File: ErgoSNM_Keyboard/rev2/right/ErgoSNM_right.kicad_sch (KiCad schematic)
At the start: 21 parts, among them J1 USB_C_Receptacle_USB2.0, J2 USB_C_Receptacle_USB2.0, J3 PJ-393_TRRS_8P, J4 Conn_01x08, U1 RT9013-33GB, U2 SRV05-4

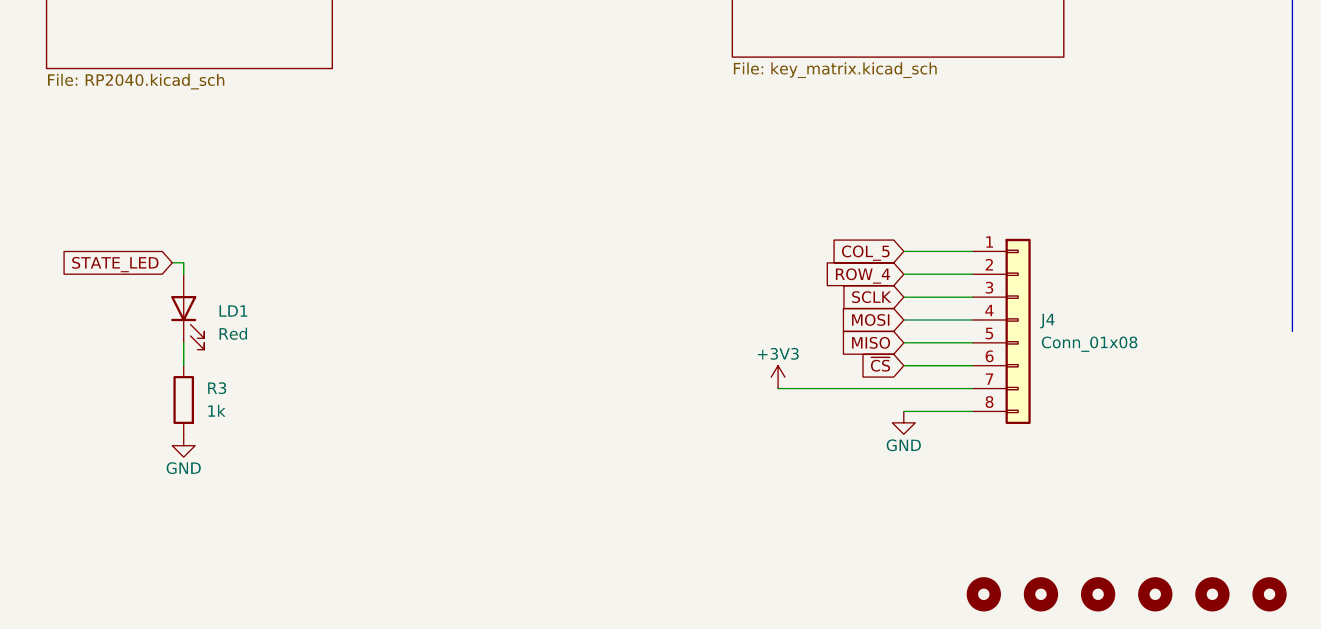
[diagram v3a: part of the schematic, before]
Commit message: Update FPC connection and add additional LED LD2
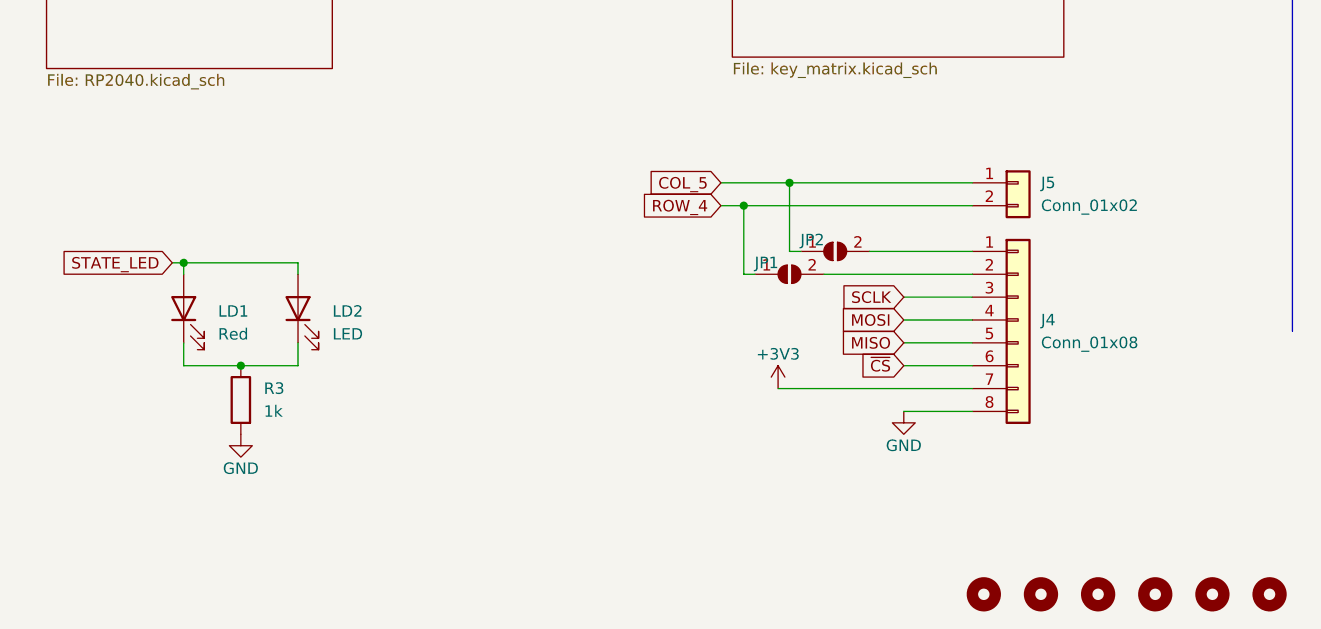
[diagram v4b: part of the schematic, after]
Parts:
- added J5: Conn_01x02, Connector_PinHeader_2.54mm:PinHeader_1x02_P2.54mm_Vertical, symbol Connector_Generic:Conn_01x02
- added JP1, JP2: SolderJumper_2_Open, Jumper:SolderJumper-2_P1.3mm_Open_TrianglePad1.0x1.5mm, symbol Jumper:SolderJumper_2_Open
- added LD2: LED, LED_SMD:LED_0805_2012Metric_Pad1.15x1.40mm_HandSolder, symbol Device:LED
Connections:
- net COL_5: now also J5.1 (Pin_1), JP2.1 (A); no longer J4.1 (Pin_1)
- net ROW_4: now also J5.2 (Pin_2), JP1.1 (A); no longer J4.2 (Pin_2)
- net STATE_LED: now also LD2.2 (A)
- net at LD1.1 (K), R3.1: now also LD2.1 (K)
- new net: J4.2 (Pin_2), JP1.2 (B)
- new net: J4.1 (Pin_1), JP2.2 (B)
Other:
- moved on the sheet: R3

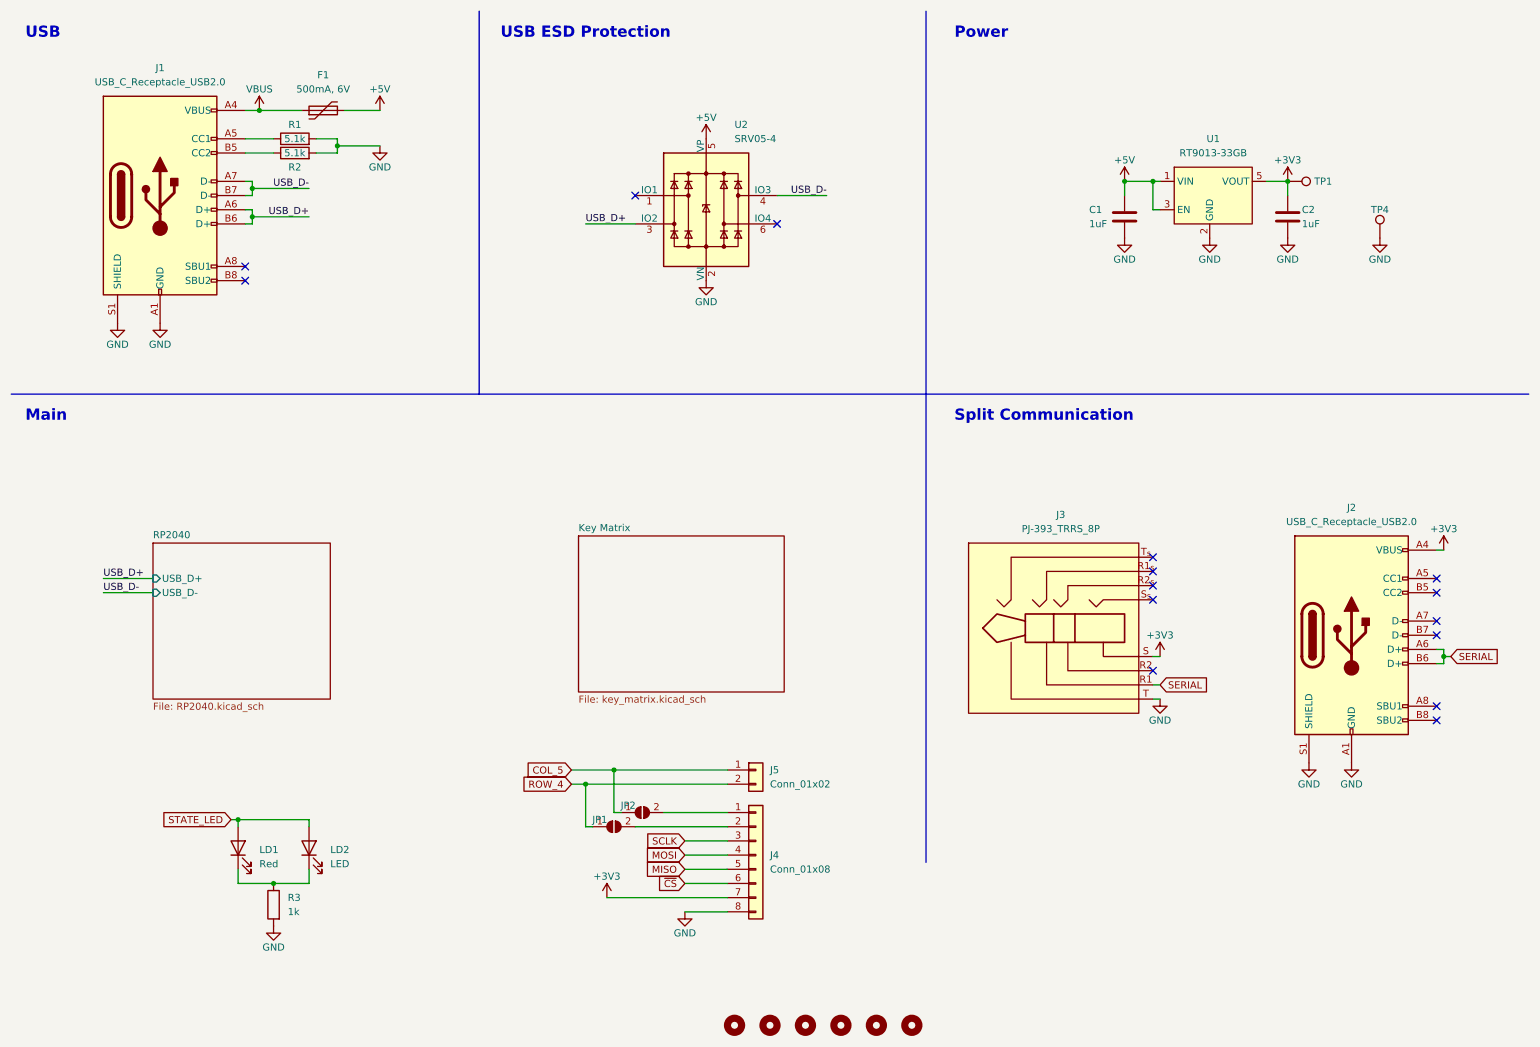
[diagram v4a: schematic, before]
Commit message: Change license to CERN-OHL-P v2
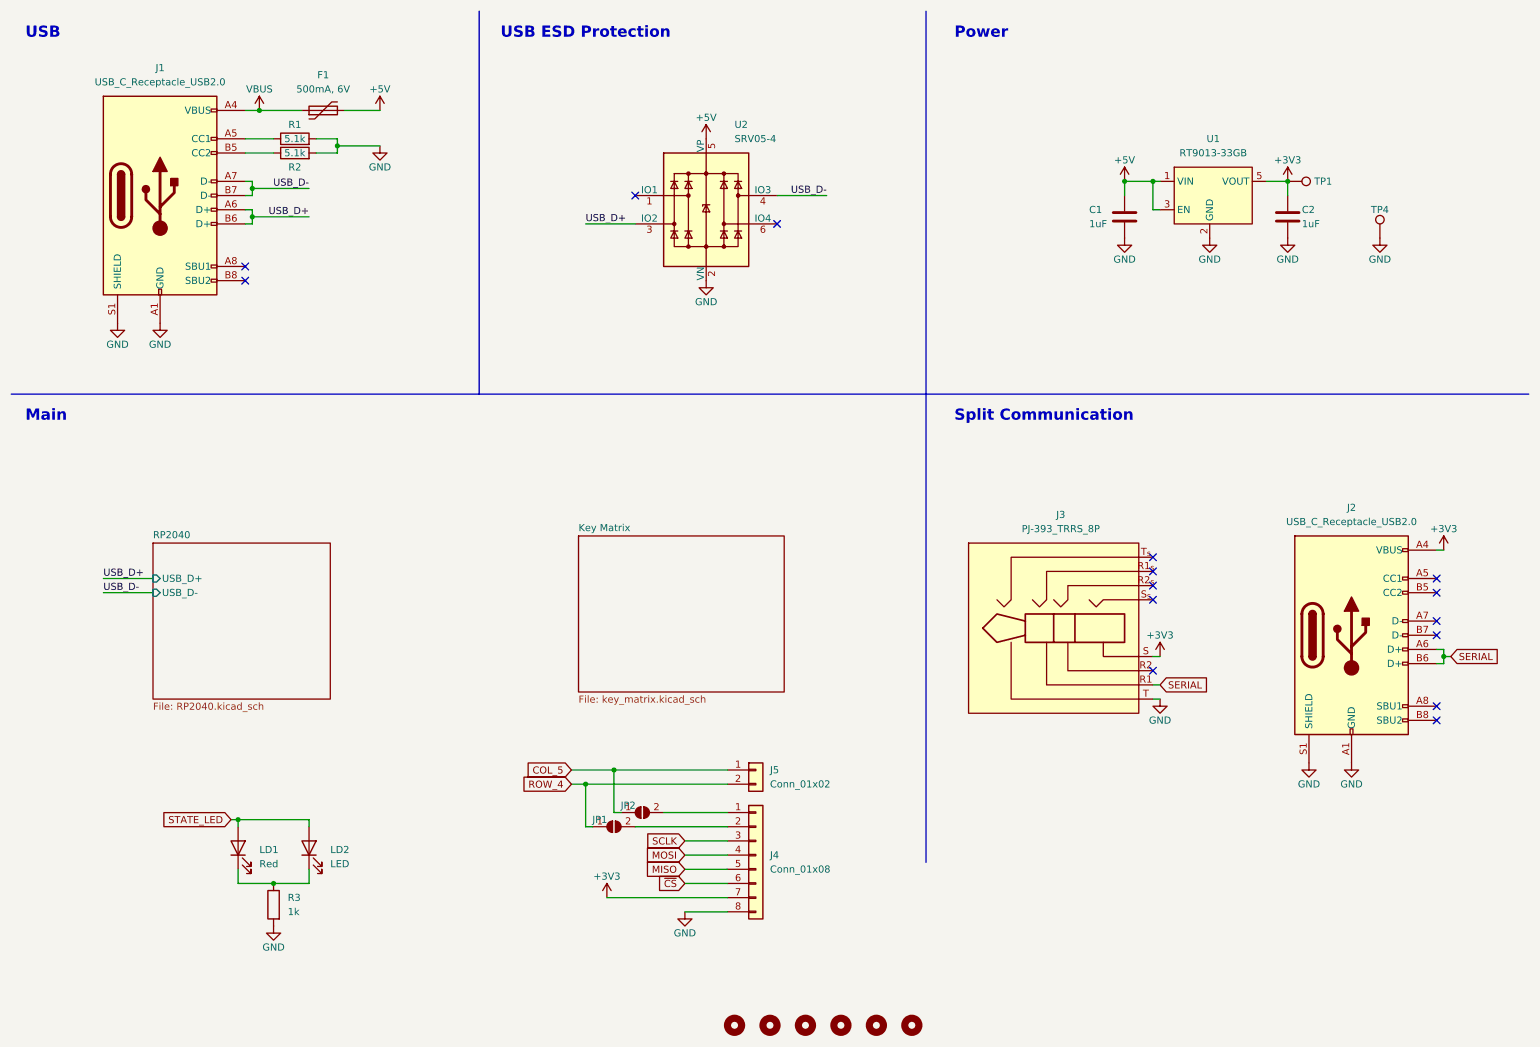
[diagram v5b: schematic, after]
